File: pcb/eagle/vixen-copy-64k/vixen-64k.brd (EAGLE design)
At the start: 89.6 x 59.5 mm, 34 parts, among them CN1 EXPANSIONPORT-VIC20-EDGEEDGE, IC1 74HCT393N, IC10 74LS30N, IC2 74AC157N, IC3 74AC157N, IC4 74AC157N, IC5 74AC157N, IC6 74ALS11N, IC8 74132N, IC9 74LS00N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

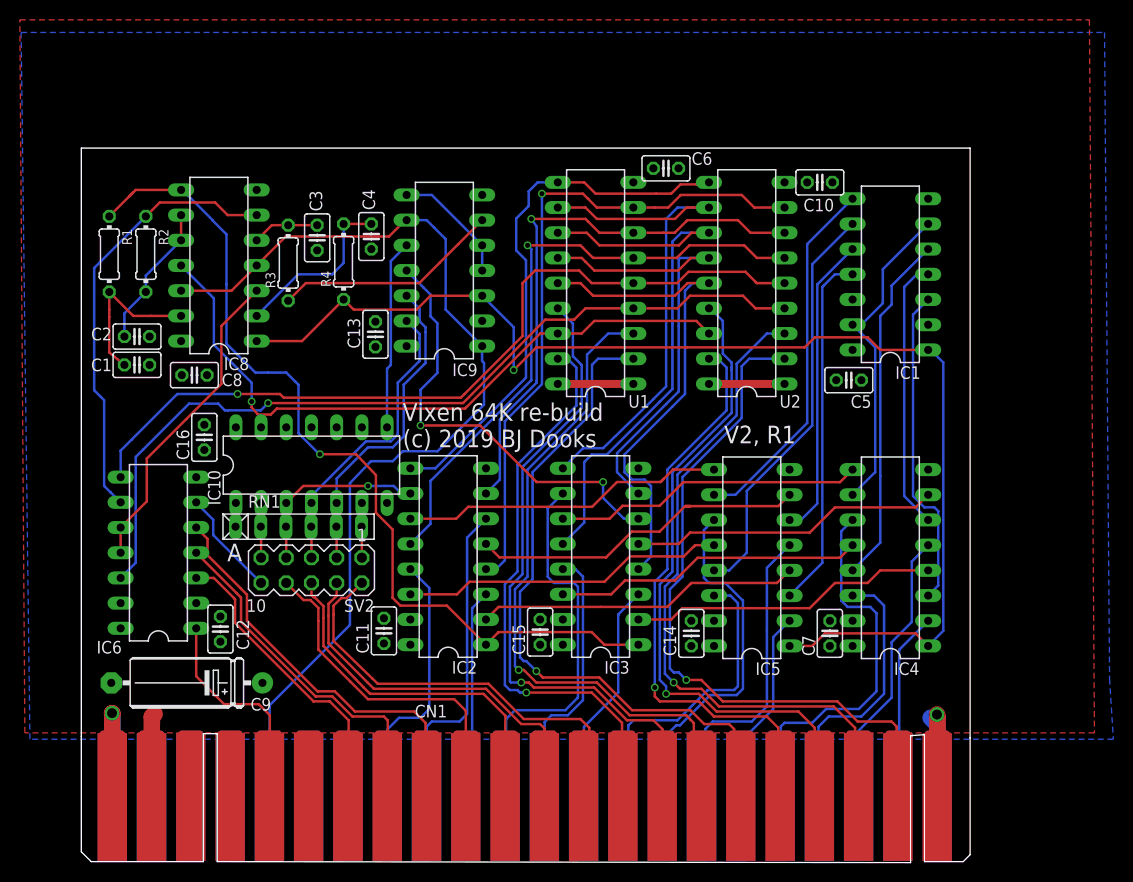
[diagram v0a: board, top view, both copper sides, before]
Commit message: vixen-64k: silkscreen updates and minor routing
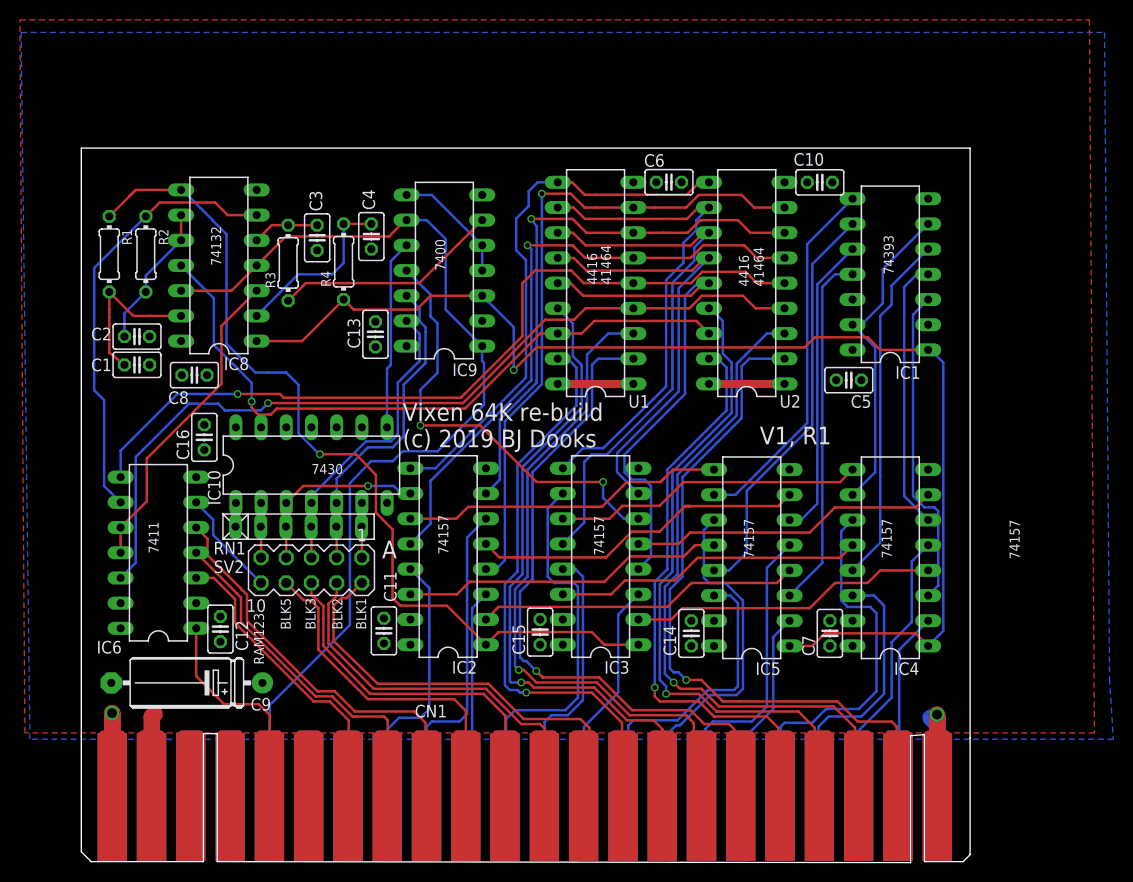
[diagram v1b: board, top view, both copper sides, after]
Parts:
- moved C6 1.43 mm to (64.0, 68.7)
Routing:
- net RA3: track 51.7 -> 49.8 mm
- net RA1: track 46.5 -> 44.8 mm
- net RA2: track 56.3 -> 54.7 mm
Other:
- board text added: "41464"
- board text added: "4416"
- board text added: "7400"
- board text added: "7411"
- board text added: "74132"
- board text added: "74157"
- board text added: "7430"
- board text added: "74393"
- board text added: "BLK1"
- board text added: "BLK2"
- board text added: "BLK3"
- board text added: "BLK5"
- board text added: "RAM123"
- board text added: "V1, R1"
- board text added: "V1, R1 6 May 2021"
- board text removed: "V2, R1"
- board text removed: "V2, R1 12 March 2019"
